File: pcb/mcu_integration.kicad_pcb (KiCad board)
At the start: 4 copper layers, 70 x 70 mm, 68 parts, among them IC1 TL7660IDGKR, IC2 TL081IDT, IC6 AD844_OPAMP_AL, IC7 FOD814_OPTO_AL, IC9 TL081IDT, J1 Conn_01x05, J4 Conn_01x02, J5 DM3BT-DSF-PEJS, M1 MountingHole_Pad, M2 MountingHole_Pad, M3 MountingHole_Pad, M4 MountingHole_Pad, U1 STM32F103RBTx, U3 REF192_AL, U6 LM35DM

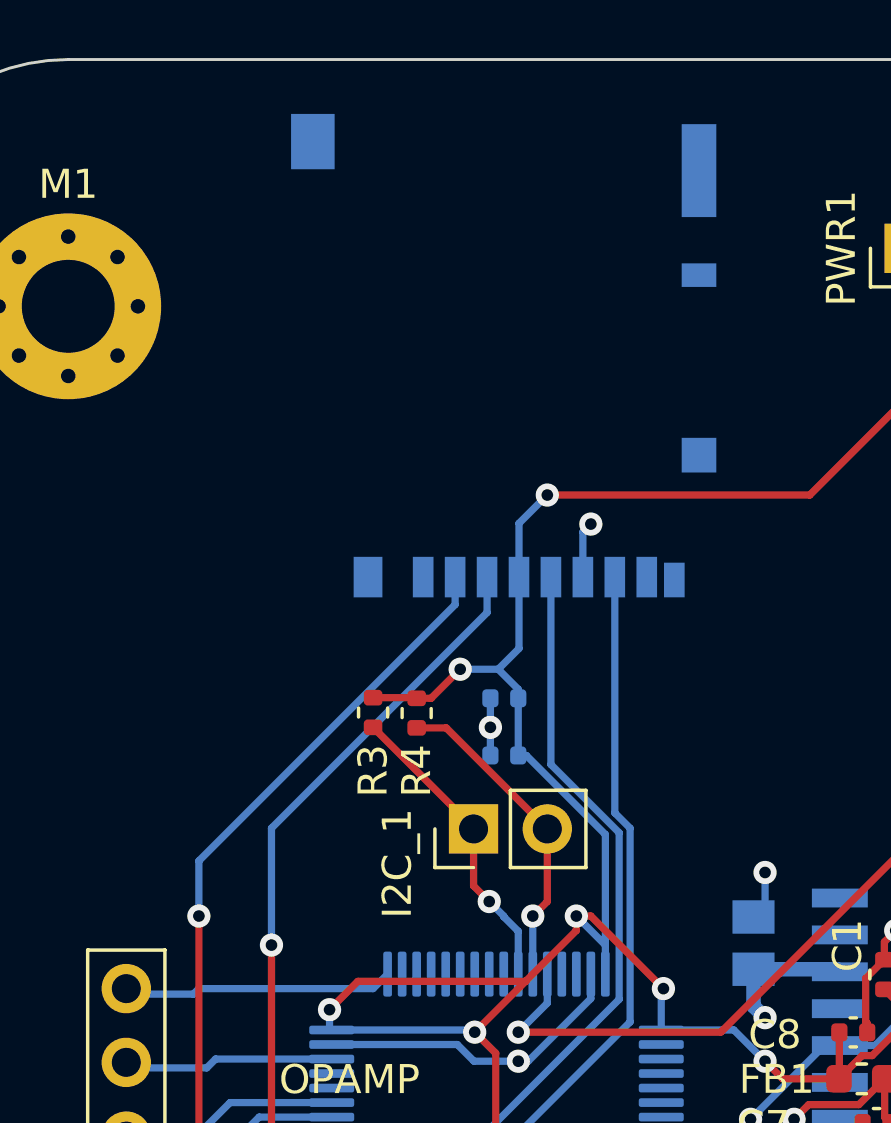
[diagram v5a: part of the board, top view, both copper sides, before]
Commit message: Added reset button & LED, fixed SD card overhang
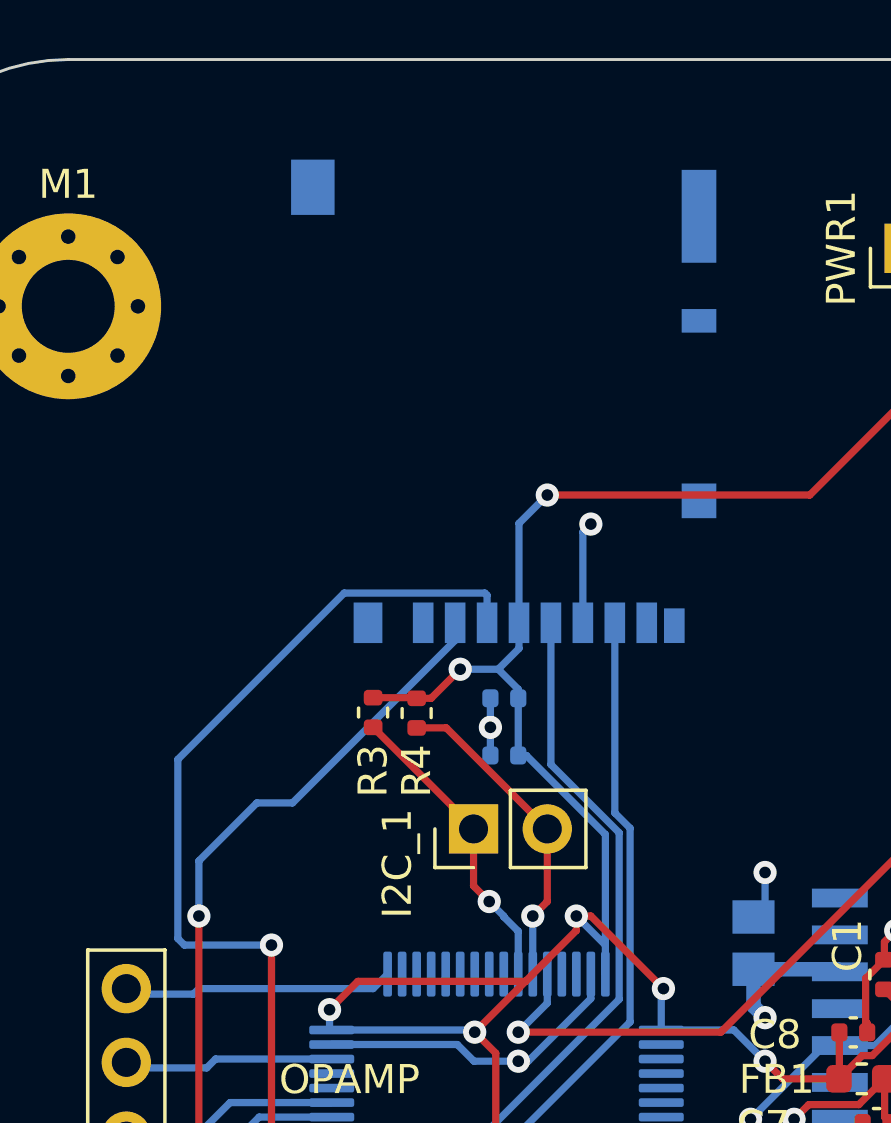
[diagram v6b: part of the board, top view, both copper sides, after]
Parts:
- C14, C15, C16, C17: value 0.1u -> 0.01u
- moved J5 1.57 mm to (125.5, 64.6)
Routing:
- net /SPI2_MOSI: track 27.6 -> 35.4 mm
- net GND: track 123.9 -> 125.5 mm
- net /SPI2_SCK: track 28.8 -> 27.2 mm
- net /SPI2_MISO: track 29.2 -> 27.6 mm
- net /SPI2_CS_NSS: track 30.8 -> 29.9 mm
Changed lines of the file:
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@@
 			)
 		)
-		(property "Value" "0.1u"
+		(property "Value" "0.01u"
 			(at 0 0 -90)
 			(unlocked yes)
@@
 			)
 		)
-		(property "Value" "0.1u"
+		(property "Value" "0.01u"
 			(at 0 0 -90)
 			(unlocked yes)
@@
 			)
 		)
-		(property "Value" "0.1u"
+		(property "Value" "0.01u"
 			(at 0 0 -90)
 			(unlocked yes)
@@
 			)
 		)
-		(property "Value" "0.1u"
+		(property "Value" "0.01u"
 			(at 0 0 -90)
 			(unlocked yes)
@@
 		(tags "Through hole pin header THT 1x04 2.54mm single row")
 		(property "Reference" "J_AD2"
-			(at 2.5 0.12 360)
+			(at 2.5 0.12 0)
 			(layer "F.SilkS")
 			(effects
@@
 		)
 		(property "Value" "Conn_01x04"
-			(at 2.794 5.08 360)
+			(at 2.794 5.08 0)
 			(layer "F.Fab")
 			(effects
@@
 		)
 		(fp_text user "${REFERENCE}"
-			(at 0 3.81 360)
+			(at 0 3.81 0)
 			(layer "F.Fab")
 			(effects
@@
 	(footprint "capstone:DM3BT_DSF_PEJS"
 		(layer "B.Cu")
-		(at 125.5 63)
+		(at 125.5 64.573599)
 		(tags "DM3BT-DSF-PEJS ")
 		(property "Reference" "J5"
@@
 	)
 	(segment
-		(start 123.825 71.7749)
+		(start 116.995802 78.604098)
 		(end 115 80.5999)
 		(width 0.25)
@@
 	)
 	(segment
-		(start 123.825 70.8264)
-		(end 123.825 71.7749)
+		(start 123.825 72.399999)
+		(end 123.825 73.004098)
+		(width 0.25)
+		(layer "B.Cu")
+		(net 5)
+	)
+	(segment
+		(start 123.825 73.004098)
+		(end 118.225 78.604098)
 		(width 0.25)
 		(layer "B.Cu")
@@
 	)
 	(segment
+		(start 118.225 78.604098)
+		(end 116.995802 78.604098)
+		(width 0.25)
+		(layer "B.Cu")
+		(net 5)
+	)
+	(segment
 		(start 115 80.5999)
 		(end 115 82.5)
@@
 	)
 	(segment
-		(start 124.925 72.049695)
-		(end 117.5 79.474695)
+		(start 124.85 71.376499)
+		(end 120.0047 71.376499)
 		(width 0.25)
 		(layer "B.Cu")
@@
 	)
 	(segment
-		(start 117.425 92.425)
-		(end 119.575 92.425)
+		(start 114.275 77.106199)
+		(end 114.275 83.275)
 		(width 0.25)
 		(layer "B.Cu")
@@
 	)
 	(segment
-		(start 124.925 70.8264)
-		(end 124.925 72.049695)
+		(start 117.425 92.425)
+		(end 119.575 92.425)
 		(width 0.25)
 		(layer "B.Cu")
@@
 	)
 	(segment
-		(start 117.5 79.474695)
+		(start 124.925 72.399999)
+		(end 124.925 71.451499)
+		(width 0.25)
+		(layer "B.Cu")
+		(net 6)
+	)
+	(segment
+		(start 120.0047 71.376499)
+		(end 114.275 77.106199)
+		(width 0.25)
+		(layer "B.Cu")
+		(net 6)
+	)
+	(segment
+		(start 114.5 83.5)
 		(end 117.5 83.5)
 		(width 0.25)
@@
 	)
 	(segment
-		(start 127.125001 70.8264)
-		(end 127.125001 77.281844)
+		(start 124.925 71.451499)
+		(end 124.85 71.376499)
 		(width 0.25)
 		(layer "B.Cu")
-		(net 7)
+		(net 6)
+	)
+	(segment
+		(start 114.275 83.275)
+		(end 114.5 83.5)
+		(width 0.25)
+		(layer "B.Cu")
+		(net 6)
 	)
 	(segment
@@
 	)
 	(segment
+		(start 127.125001 77.281844)
+		(end 127.125001 72.399999)
+		(width 0.25)
+		(layer "B.Cu")
+		(net 7)
+	)
+	(segment
 		(start 124.5 92)
 		(end 121.5 92)
@@
 	)
 	(segment
-		(start 121.075 92.925)
-		(end 119.575 92.925)
+		(start 129.324999 78.948684)
+		(end 129.324999 72.399999)
 		(width 0.25)
 		(layer "B.Cu")
@@
 	)
 	(segment
-		(start 129.324999 70.8264)
-		(end 129.324999 78.948684)
+		(start 121.075 92.925)
+		(end 119.575 92.925)
 		(width 0.25)
 		(layer "B.Cu")
@@
 	)
 	(segment
+		(start 126.025 72.399999)
+		(end 126.025 73.284999)
+		(width 0.25)
+		(layer "B.Cu")
+		(net 60)
+	)
+	(segment
 		(start 122.507236 94)
 		(end 123 94)
@@
 	)
 	(segment
+		(start 126.025 73.284999)
+		(end 125.309999 74)
+		(width 0.25)
+		(layer "B.Cu")
+		(net 60)
+	)
+	(segment
 		(start 128 95.85)
 		(end 128 95)
@@
 	)
 	(segment
-		(start 126.025 70.8264)
-		(end 126.025 73.284999)
+		(start 126.025 72.399999)
+		(end 126.025 68.975)
 		(width 0.25)
 		(layer "B.Cu")
@@
 	)
 	(segment
-		(start 126.025 73.284999)
-		(end 125.309999 74)
-		(width 0.25)
-		(layer "B.Cu")
-		(net 60)
-	)
-	(segment
 		(start 125.309999 74)
 		(end 126 74.690001)
@@
 	)
 	(segment
-		(start 126.025 68.975)
-		(end 126.025 70.8264)
-		(width 0.25)
-		(layer "B.Cu")
-		(net 60)
-	)
-	(segment
 		(start 133.425 86.425)
 		(end 130.925 86.425)
@@
 	)
 	(segment
-		(start 128.225001 70.8264)
-		(end 128.225001 69.274999)
-		(width 0.25)
-		(layer "B.Cu")
-		(net 86)
-	)
-	(segment
 		(start 125.04 76)
 		(end 125.04 75)
@@
 	)
 	(segment
+		(start 128.225001 72.399999)
+		(end 128.225001 69.274999)
+		(width 0.25)
+		(layer "B.Cu")
+		(net 86)
+	)
+	(segment
 		(start 136.962 95.723)
 		(end 136.962 93.538)
@@
 	)
 	(segment
+		(start 128.225001 69.274999)
+		(end 128.5 69)
+		(width 0.25)
+		(layer "B.Cu")
+		(net 86)
+	)
+	(segment
 		(start 119.575 86.925)
 		(end 123.899695 86.925)
@@
 		(width 0.25)
 		(layer "B.Cu")
-		(net 86)
-	)
-	(segment
-		(start 128.225001 69.274999)
-		(end 128.5 69)
-		(width 0.25)
-		(layer "B.Cu")

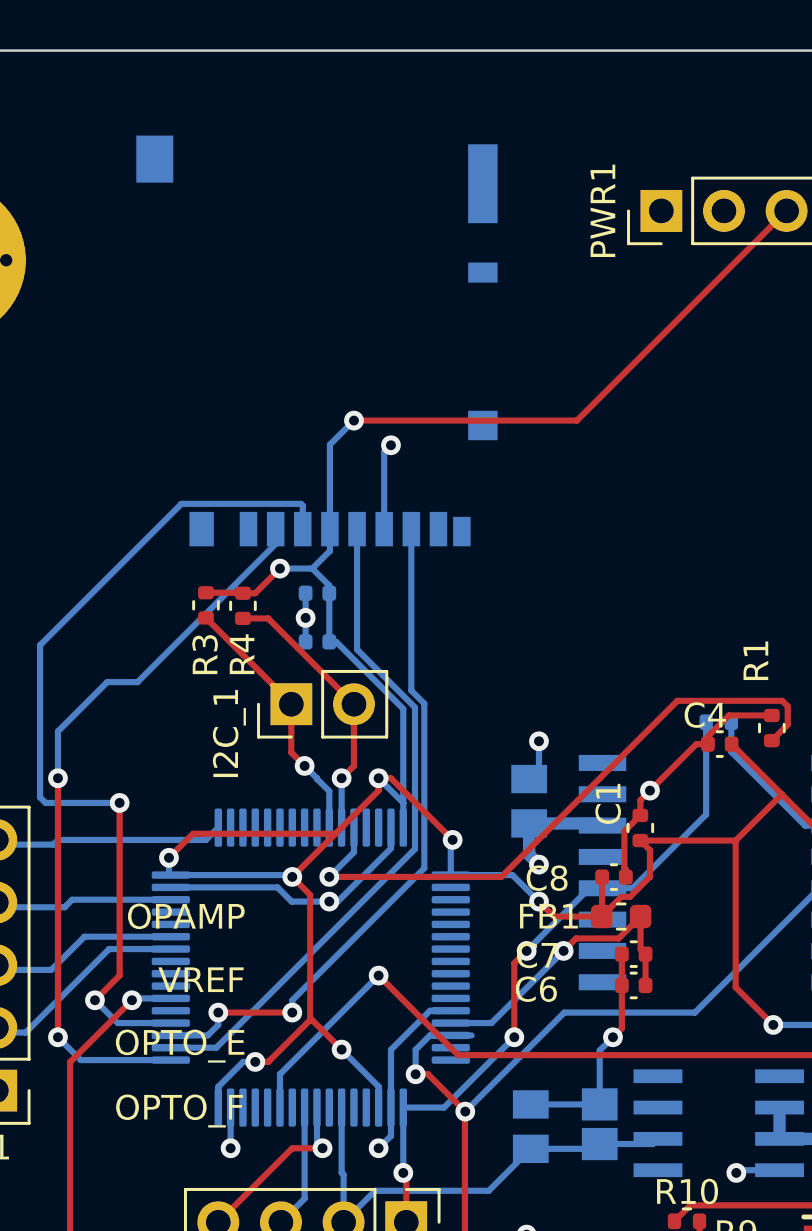
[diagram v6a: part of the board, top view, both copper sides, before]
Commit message: Added reset button & LED, fixed SD card overhang
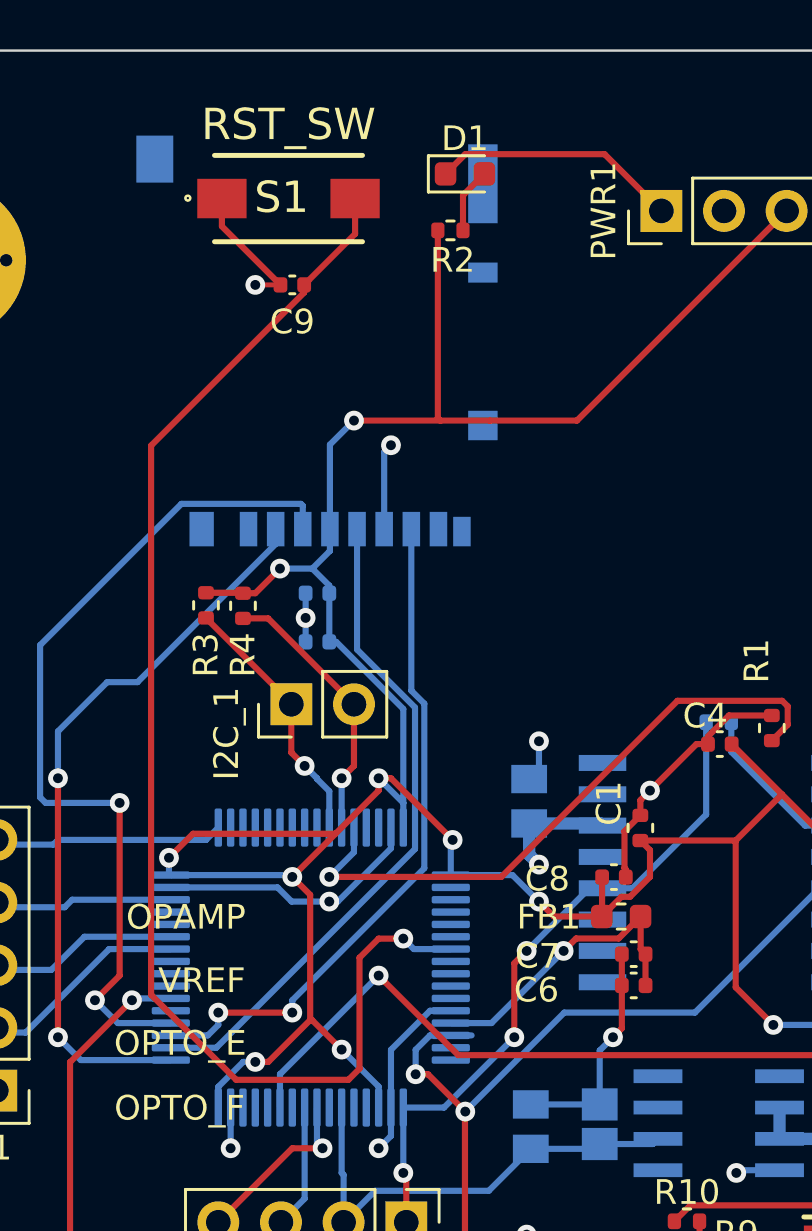
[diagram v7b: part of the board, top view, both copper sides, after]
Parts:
- added C9: 100n, Capacitor_SMD:C_0402_1005Metric, F.Cu at (124.5, 62.5)
- added D1: RED, LED_SMD:LED_0603_1608Metric, F.Cu at (131.5, 58.0)
- added R2: 2.2k, Resistor_SMD:R_0402_1005Metric, F.Cu at (130.9, 60.3)
- added S1: RST_SW, capstone:95C04A3GWRT, F.Cu at (124.3, 59.0)
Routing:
- net /NRST: track 0.00 -> 54.5 mm, vias 0 -> 1
- net GND: track 125.5 -> 140.0 mm, vias 20 -> 21
- net 3.3V Output: track 142.5 -> 150.2 mm
- net Net-(D1-A): track 0.00 -> 2.65 mm

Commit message: Added non-inverting amplifier
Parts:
- removed C45, C46: 0.1u, capstone:CAPC220145_88N_KEM-0.1u
- removed IC9: TL081IDT, capstone:SOIC127P600X175-8N
- removed R11, R12: 10K, Resistor_SMD:R_0402_1005Metric
- C14, C15, C16, C17: value 0.01u -> 0.47u
- R10: value 15K -> 9K
- R5, R6, R7, R8: value 100K -> 3.3K
- R9: value 10K -> 1K
- moved R10 19.9 mm to (157.6, 110.7), turned to 90 degrees
- moved C44 15.9 mm to (155.4, 115.7), turned to 0 degrees
- moved R9 15.8 mm to (155.9, 106.2)
- moved C18 14.4 mm to (152.7, 104.6)
- moved IC2 9.28 mm to (153.9, 110.5), turned to -90 degrees
- moved J4 2.65 mm to (162.3, 108.8)
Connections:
- C44 pad 1: -5V Output -> +5V
- IC2 pad 3: GND -> RC_OUTPUT
- IC2 pad 6: INVERT_SINE -> ADC1_IN0_SINE
- R10 pad 1: INVERT_SINE -> ADC1_IN0_SINE
- R9 pad 1: RC_OUTPUT -> Net-(IC2-INVERTING_INPUT)
- R9 pad 2: Net-(IC2-INVERTING_INPUT) -> GND
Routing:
- net GND: track 140.0 -> 112.0 mm, vias 21 -> 22
- net -5V Output: track 80.4 -> 58.2 mm, vias 4 -> 2
- net INVERT_SINE: track 18.3 -> 0.00 mm
- net RC_OUTPUT: track 39.2 -> 53.5 mm
- net Net-(IC9-INVERTING_INPUT): track 13.6 -> 0.00 mm
- net +5V: track 34.8 -> 22.5 mm
- net ADC1_IN0_SINE: track 88.8 -> 84.4 mm, vias 6 -> 5
- net Net-(IC2-INVERTING_INPUT): track 7.09 -> 6.47 mm
